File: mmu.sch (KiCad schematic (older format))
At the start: 6 parts

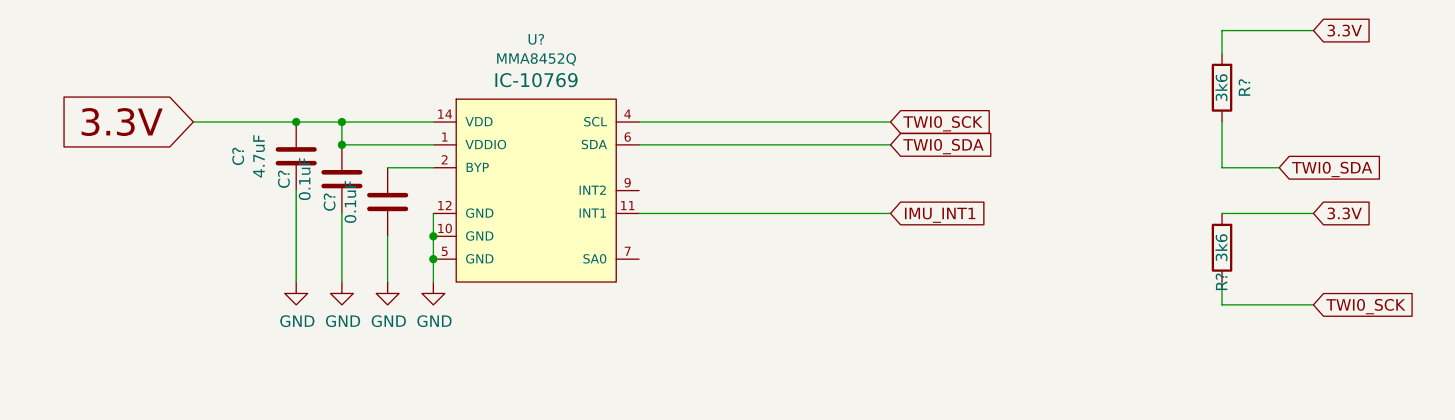
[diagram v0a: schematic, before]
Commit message: MMU Schematic rework.
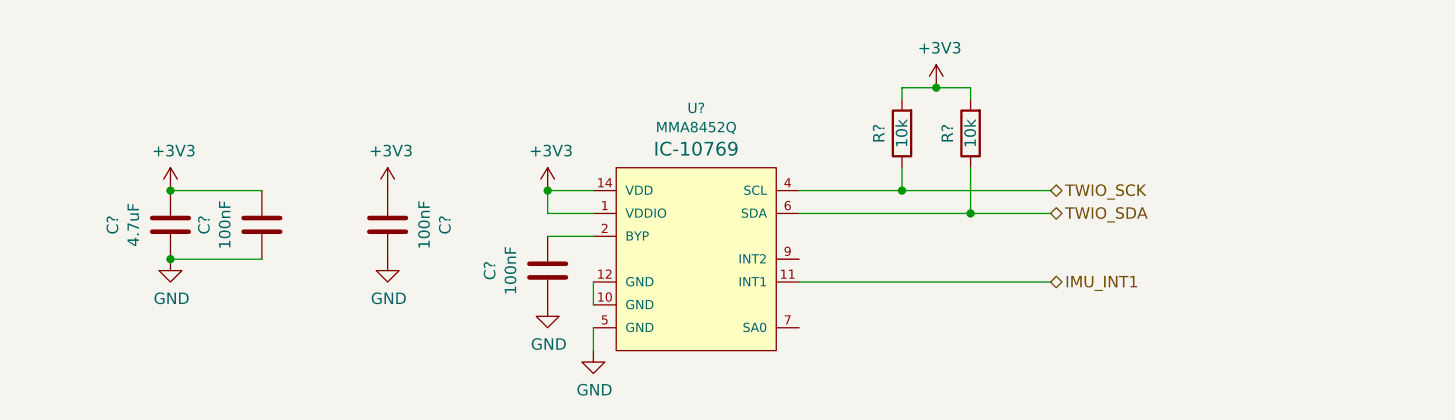
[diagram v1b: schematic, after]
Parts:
- removed C? (x2): 0.1uF, Capacitor_SMD:C_0603_1608Metric, symbol Device:C
- removed R?: 3k6, Resistors:0603, symbol Device:R
- added C? (x3): 100nF, Capacitor_SMD:C_0603_1608Metric, symbol Device:C
- added R?: 10k, Resistors:0603, symbol Device:R
- R?: value 3k6 -> 10k
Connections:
- net GND: now also C?.1, C?.2, C?.2; no longer U?.10 (GND), U?.12 (GND)
- net at U?.2 (BYP): now also C?.1
- net 3.3V renamed +3V3
- net +3V3: now also C?.1, C?.2, R?.2
- net TWI0_SCK renamed TWIO_SCK
- net TWIO_SCK: now also R?.1
- net TWI0_SDA renamed TWIO_SDA
- net TWIO_SDA: now also R?.1; no longer R?.1
- new net: U?.10 (GND), U?.12 (GND)
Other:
- moved on the sheet: C?, R?, U?

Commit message: Modem schematic updated.
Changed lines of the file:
@@
 $Descr A4 11693 8268
 encoding utf-8
-Sheet 5 6
+Sheet 4 6
 Title ""
 Date ""
@@
 Text HLabel 7400 3700 2    50   BiDi ~ 0
 TWIO_SDA
-Text HLabel 7400 4000 2    50   BiDi ~ 0
+Text HLabel 7400 4000 2    50   Output ~ 0
 IMU_INT1
 $Comp

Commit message: Power Sch. Updated.
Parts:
- gave numbers to parts that had none: 7
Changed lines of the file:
@@
 P 5850 3900
 AR Path="/6061C78B" Ref="U?"  Part="1"
-AR Path="/606146CD/6061C78B" Ref="U?"  Part="1"
-F 0 "U?" H 5850 4560 45  0000 C CNN
+AR Path="/606146CD/6061C78B" Ref="U8"  Part="1"
+F 0 "U8" H 5850 4560 45  0000 C CNN
 F 1 "MMA8452Q" H 5850 4476 45  0000 C CNN
 F 2 "QFN-16" H 5850 4400 20  0001 C CNN
@@
 P 3550 3750
 AR Path="/6061C792" Ref="C?"  Part="1"
-AR Path="/606146CD/6061C792" Ref="C?"  Part="1"
-F 0 "C?" V 3298 3750 50  0000 C CNN
+AR Path="/606146CD/6061C792" Ref="C36"  Part="1"
+F 0 "C36" V 3298 3750 50  0000 C CNN
 F 1 "4.7uF" V 3389 3750 50  0000 C CNN
 F 2 "Capacitor_SMD:C_0603_1608Metric" H 3588 3600 50  0001 C CNN
@@
 P 5200 4100
 AR Path="/6061C7BB" Ref="#PWR?"  Part="1"
-AR Path="/606146CD/6061C7BB" Ref="#PWR?"  Part="1"
-F 0 "#PWR?" H 5200 3850 50  0001 C CNN
+AR Path="/606146CD/6061C7BB" Ref="#PWR058"  Part="1"
+F 0 "#PWR058" H 5200 3850 50  0001 C CNN
 F 1 "GND" H 5205 3927 50  0000 C CNN
 F 2 "" H 5200 4100 50  0001 C CNN
@@
 P 5400 4300
 AR Path="/6061C7C5" Ref="#PWR?"  Part="1"
-AR Path="/606146CD/6061C7C5" Ref="#PWR?"  Part="1"
-F 0 "#PWR?" H 5400 4050 50  0001 C CNN
+AR Path="/606146CD/6061C7C5" Ref="#PWR059"  Part="1"
+F 0 "#PWR059" H 5400 4050 50  0001 C CNN
 F 1 "GND" H 5405 4127 50  0000 C CNN
 F 2 "" H 5400 4300 50  0001 C CNN
@@
 P 6750 3350
 AR Path="/60620D77" Ref="R?"  Part="1"
-AR Path="/606146CD/60620D77" Ref="R?"  Part="1"
-F 0 "R?" V 6850 3350 50  0000 C CNN
+AR Path="/606146CD/60620D77" Ref="R18"  Part="1"
+F 0 "R18" V 6850 3350 50  0000 C CNN
 F 1 "10k" V 6750 3350 50  0000 C CNN
 F 2 "Resistors:0603" V 6680 3350 50  0001 C CNN
@@
 	5400 4000 5400 4100
 $Comp
-L power:+3V3 #PWR?
+L power:+3V3 #PWR060
 U 1 1 604099B4
 P 6900 3150
-F 0 "#PWR?" H 6900 3000 50  0001 C CNN
+F 0 "#PWR060" H 6900 3000 50  0001 C CNN
 F 1 "+3V3" H 6915 3323 50  0000 C CNN
 F 2 "" H 6900 3150 50  0001 C CNN
@@
 P 7050 3350
 AR Path="/6040B1A1" Ref="R?"  Part="1"
-AR Path="/606146CD/6040B1A1" Ref="R?"  Part="1"
-F 0 "R?" V 7150 3350 50  0000 C CNN
+AR Path="/606146CD/6040B1A1" Ref="R19"  Part="1"
+F 0 "R19" V 7150 3350 50  0000 C CNN
 F 1 "10k" V 7050 3350 50  0000 C CNN
 F 2 "Resistors:0603" V 6980 3350 50  0001 C CNN
@@
 	7050 3700 7400 3700
 $Comp
-L power:+3V3 #PWR?
+L power:+3V3 #PWR057
 U 1 1 6040D137
 P 5200 3600
-F 0 "#PWR?" H 5200 3450 50  0001 C CNN
+F 0 "#PWR057" H 5200 3450 50  0001 C CNN
 F 1 "+3V3" H 5215 3773 50  0000 C CNN
 F 2 "" H 5200 3600 50  0001 C CNN
@@
 Connection ~ 5200 3600
 $Comp
-L power:+3V3 #PWR?
+L power:+3V3 #PWR053
 U 1 1 60412212
 P 3550 3600
-F 0 "#PWR?" H 3550 3450 50  0001 C CNN
+F 0 "#PWR053" H 3550 3450 50  0001 C CNN
 F 1 "+3V3" H 3565 3773 50  0000 C CNN
 F 2 "" H 3550 3600 50  0001 C CNN
@@
 $EndComp
 $Comp
-L power:+3V3 #PWR?
+L power:+3V3 #PWR055
 U 1 1 60415A29
 P 4500 3600
-F 0 "#PWR?" H 4500 3450 50  0001 C CNN
+F 0 "#PWR055" H 4500 3450 50  0001 C CNN
 F 1 "+3V3" H 4515 3773 50  0000 C CNN
 F 2 "" H 4500 3600 50  0001 C CNN
@@
 P 3550 3900
 AR Path="/60416437" Ref="#PWR?"  Part="1"
-AR Path="/606146CD/60416437" Ref="#PWR?"  Part="1"
-F 0 "#PWR?" H 3550 3650 50  0001 C CNN
+AR Path="/606146CD/60416437" Ref="#PWR054"  Part="1"
+F 0 "#PWR054" H 3550 3650 50  0001 C CNN
 F 1 "GND" H 3555 3727 50  0000 C CNN
 F 2 "" H 3550 3900 50  0001 C CNN
@@
 P 4500 3900
 AR Path="/6041677D" Ref="#PWR?"  Part="1"
-AR Path="/606146CD/6041677D" Ref="#PWR?"  Part="1"
-F 0 "#PWR?" H 4500 3650 50  0001 C CNN
+AR Path="/606146CD/6041677D" Ref="#PWR056"  Part="1"
+F 0 "#PWR056" H 4500 3650 50  0001 C CNN
 F 1 "GND" H 4505 3727 50  0000 C CNN
 F 2 "" H 4500 3900 50  0001 C CNN
@@
 AR Path="/6044E3D1" Ref="C?"  Part="1"
 AR Path="/603B75FA/6044E3D1" Ref="C?"  Part="1"
-AR Path="/606146CD/6044E3D1" Ref="C?"  Part="1"
-F 0 "C?" V 4248 3750 50  0000 C CNN
+AR Path="/606146CD/6044E3D1" Ref="C38"  Part="1"
+F 0 "C38" V 4248 3750 50  0000 C CNN
 F 1 "100nF" V 4339 3750 50  0000 C CNN
 F 2 "Capacitor_SMD:C_0603_1608Metric" H 4538 3600 50  0001 C CNN
@@
 AR Path="/6045277F" Ref="C?"  Part="1"
 AR Path="/603B75FA/6045277F" Ref="C?"  Part="1"
-AR Path="/606146CD/6045277F" Ref="C?"  Part="1"
-F 0 "C?" V 3698 3750 50  0000 C CNN
+AR Path="/606146CD/6045277F" Ref="C37"  Part="1"
+F 0 "C37" V 3698 3750 50  0000 C CNN
 F 1 "100nF" V 3789 3750 50  0000 C CNN
 F 2 "Capacitor_SMD:C_0603_1608Metric" H 3988 3600 50  0001 C CNN
@@
 AR Path="/604535B4" Ref="C?"  Part="1"
 AR Path="/603B75FA/604535B4" Ref="C?"  Part="1"
-AR Path="/606146CD/604535B4" Ref="C?"  Part="1"
-F 0 "C?" V 4948 3950 50  0000 C CNN
+AR Path="/606146CD/604535B4" Ref="C39"  Part="1"
+F 0 "C39" V 4948 3950 50  0000 C CNN
 F 1 "100nF" V 5039 3950 50  0000 C CNN
 F 2 "Capacitor_SMD:C_0603_1608Metric" H 5238 3800 50  0001 C CNN

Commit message: Power section placement completed.
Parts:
- R22: renamed from R18; footprint Resistors:0603 -> Resistor_SMD:R_0603_1608Metric
- R23: renamed from R19; footprint Resistors:0603 -> Resistor_SMD:R_0603_1608Metric
- renumbered C36 to C40, C37 to C41, C38 to C42, C39 to C43
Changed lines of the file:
@@
 P 3550 3750
 AR Path="/6061C792" Ref="C?"  Part="1"
-AR Path="/606146CD/6061C792" Ref="C36"  Part="1"
-F 0 "C36" V 3298 3750 50  0000 C CNN
+AR Path="/606146CD/6061C792" Ref="C40"  Part="1"
+F 0 "C40" V 3298 3750 50  0000 C CNN
 F 1 "4.7uF" V 3389 3750 50  0000 C CNN
 F 2 "Capacitor_SMD:C_0603_1608Metric" H 3588 3600 50  0001 C CNN
@@
 P 5200 4100
 AR Path="/6061C7BB" Ref="#PWR?"  Part="1"
-AR Path="/606146CD/6061C7BB" Ref="#PWR058"  Part="1"
-F 0 "#PWR058" H 5200 3850 50  0001 C CNN
+AR Path="/606146CD/6061C7BB" Ref="#PWR067"  Part="1"
+F 0 "#PWR067" H 5200 3850 50  0001 C CNN
 F 1 "GND" H 5205 3927 50  0000 C CNN
 F 2 "" H 5200 4100 50  0001 C CNN
@@
 P 5400 4300
 AR Path="/6061C7C5" Ref="#PWR?"  Part="1"
-AR Path="/606146CD/6061C7C5" Ref="#PWR059"  Part="1"
-F 0 "#PWR059" H 5400 4050 50  0001 C CNN
+AR Path="/606146CD/6061C7C5" Ref="#PWR068"  Part="1"
+F 0 "#PWR068" H 5400 4050 50  0001 C CNN
 F 1 "GND" H 5405 4127 50  0000 C CNN
 F 2 "" H 5400 4300 50  0001 C CNN
@@
 P 6750 3350
 AR Path="/60620D77" Ref="R?"  Part="1"
-AR Path="/606146CD/60620D77" Ref="R18"  Part="1"
-F 0 "R18" V 6850 3350 50  0000 C CNN
+AR Path="/606146CD/60620D77" Ref="R22"  Part="1"
+F 0 "R22" V 6850 3350 50  0000 C CNN
 F 1 "10k" V 6750 3350 50  0000 C CNN
-F 2 "Resistors:0603" V 6680 3350 50  0001 C CNN
+F 2 "Resistor_SMD:R_0603_1608Metric" V 6680 3350 50  0001 C CNN
 F 3 "~" H 6750 3350 50  0001 C CNN
 	1    6750 3350
@@
 	5400 4000 5400 4100
 $Comp
-L power:+3V3 #PWR060
+L power:+3V3 #PWR069
 U 1 1 604099B4
 P 6900 3150
-F 0 "#PWR060" H 6900 3000 50  0001 C CNN
+F 0 "#PWR069" H 6900 3000 50  0001 C CNN
 F 1 "+3V3" H 6915 3323 50  0000 C CNN
 F 2 "" H 6900 3150 50  0001 C CNN
@@
 P 7050 3350
 AR Path="/6040B1A1" Ref="R?"  Part="1"
-AR Path="/606146CD/6040B1A1" Ref="R19"  Part="1"
-F 0 "R19" V 7150 3350 50  0000 C CNN
+AR Path="/606146CD/6040B1A1" Ref="R23"  Part="1"
+F 0 "R23" V 7150 3350 50  0000 C CNN
 F 1 "10k" V 7050 3350 50  0000 C CNN
-F 2 "Resistors:0603" V 6980 3350 50  0001 C CNN
+F 2 "Resistor_SMD:R_0603_1608Metric" V 6980 3350 50  0001 C CNN
 F 3 "~" H 7050 3350 50  0001 C CNN
 	1    7050 3350
@@
 	7050 3700 7400 3700
 $Comp
-L power:+3V3 #PWR057
+L power:+3V3 #PWR066
 U 1 1 6040D137
 P 5200 3600
-F 0 "#PWR057" H 5200 3450 50  0001 C CNN
+F 0 "#PWR066" H 5200 3450 50  0001 C CNN
 F 1 "+3V3" H 5215 3773 50  0000 C CNN
 F 2 "" H 5200 3600 50  0001 C CNN
@@
 Connection ~ 5200 3600
 $Comp
-L power:+3V3 #PWR053
+L power:+3V3 #PWR062
 U 1 1 60412212
 P 3550 3600
-F 0 "#PWR053" H 3550 3450 50  0001 C CNN
+F 0 "#PWR062" H 3550 3450 50  0001 C CNN
 F 1 "+3V3" H 3565 3773 50  0000 C CNN
 F 2 "" H 3550 3600 50  0001 C CNN
@@
 $EndComp
 $Comp
-L power:+3V3 #PWR055
+L power:+3V3 #PWR064
 U 1 1 60415A29
 P 4500 3600
-F 0 "#PWR055" H 4500 3450 50  0001 C CNN
+F 0 "#PWR064" H 4500 3450 50  0001 C CNN
 F 1 "+3V3" H 4515 3773 50  0000 C CNN
 F 2 "" H 4500 3600 50  0001 C CNN
@@
 P 3550 3900
 AR Path="/60416437" Ref="#PWR?"  Part="1"
-AR Path="/606146CD/60416437" Ref="#PWR054"  Part="1"
-F 0 "#PWR054" H 3550 3650 50  0001 C CNN
+AR Path="/606146CD/60416437" Ref="#PWR063"  Part="1"
+F 0 "#PWR063" H 3550 3650 50  0001 C CNN
 F 1 "GND" H 3555 3727 50  0000 C CNN
 F 2 "" H 3550 3900 50  0001 C CNN
@@
 P 4500 3900
 AR Path="/6041677D" Ref="#PWR?"  Part="1"
-AR Path="/606146CD/6041677D" Ref="#PWR056"  Part="1"
-F 0 "#PWR056" H 4500 3650 50  0001 C CNN
+AR Path="/606146CD/6041677D" Ref="#PWR065"  Part="1"
+F 0 "#PWR065" H 4500 3650 50  0001 C CNN
 F 1 "GND" H 4505 3727 50  0000 C CNN
 F 2 "" H 4500 3900 50  0001 C CNN
@@
 AR Path="/6044E3D1" Ref="C?"  Part="1"
 AR Path="/603B75FA/6044E3D1" Ref="C?"  Part="1"
-AR Path="/606146CD/6044E3D1" Ref="C38"  Part="1"
-F 0 "C38" V 4248 3750 50  0000 C CNN
+AR Path="/606146CD/6044E3D1" Ref="C42"  Part="1"
+F 0 "C42" V 4248 3750 50  0000 C CNN
 F 1 "100nF" V 4339 3750 50  0000 C CNN
 F 2 "Capacitor_SMD:C_0603_1608Metric" H 4538 3600 50  0001 C CNN
@@
 AR Path="/6045277F" Ref="C?"  Part="1"
 AR Path="/603B75FA/6045277F" Ref="C?"  Part="1"
-AR Path="/606146CD/6045277F" Ref="C37"  Part="1"
-F 0 "C37" V 3698 3750 50  0000 C CNN
+AR Path="/606146CD/6045277F" Ref="C41"  Part="1"
+F 0 "C41" V 3698 3750 50  0000 C CNN
 F 1 "100nF" V 3789 3750 50  0000 C CNN
 F 2 "Capacitor_SMD:C_0603_1608Metric" H 3988 3600 50  0001 C CNN
@@
 AR Path="/604535B4" Ref="C?"  Part="1"
 AR Path="/603B75FA/604535B4" Ref="C?"  Part="1"
-AR Path="/606146CD/604535B4" Ref="C39"  Part="1"
-F 0 "C39" V 4948 3950 50  0000 C CNN
+AR Path="/606146CD/604535B4" Ref="C43"  Part="1"
+F 0 "C43" V 4948 3950 50  0000 C CNN
 F 1 "100nF" V 5039 3950 50  0000 C CNN
 F 2 "Capacitor_SMD:C_0603_1608Metric" H 5238 3800 50  0001 C CNN

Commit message: PCB design updated.
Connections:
- net GND: now also U8.10 (GND), U8.12 (GND)
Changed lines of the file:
@@
 	1    0    0    -1
 $EndComp
+Wire Wire Line
+	5400 4100 5400 4200
+Connection ~ 5400 4100
+Connection ~ 5400 4200
 $EndSCHEMATC
